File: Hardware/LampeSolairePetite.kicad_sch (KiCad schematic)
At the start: 30 parts, among them J1 CONN_ICSP, J2 Battery connector, J3 Connector_4p_r, P1 GREEN, P2 GREEN, P3 RED, P4 GREEN, U1 NCP114, U2 PIC16F1827

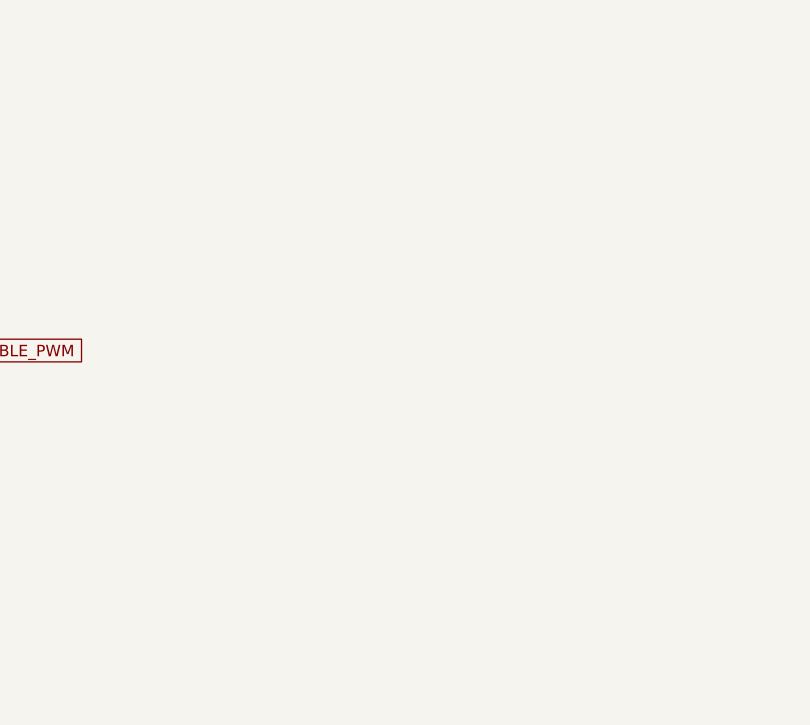
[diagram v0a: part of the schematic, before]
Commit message: Renamed files
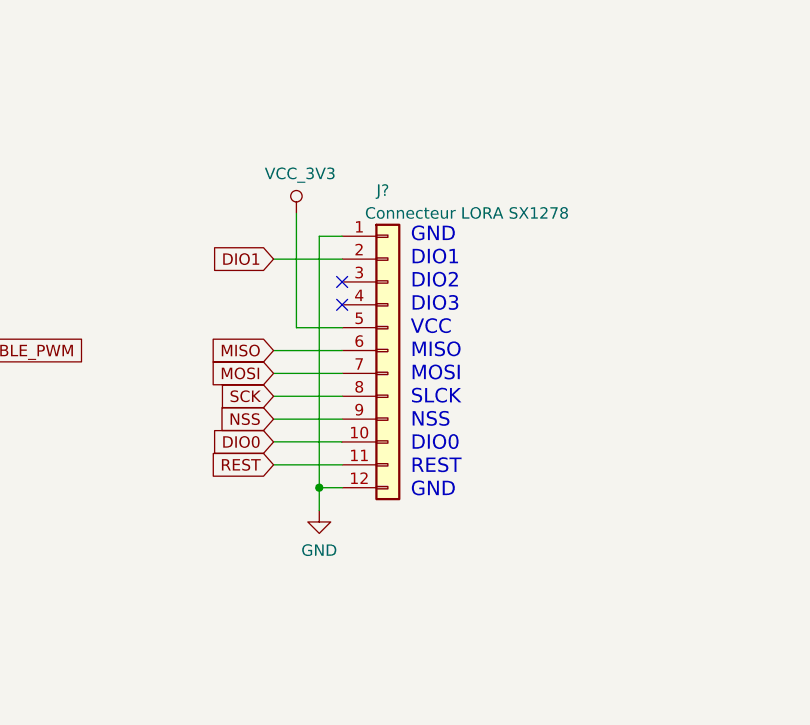
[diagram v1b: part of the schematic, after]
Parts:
- added J?: Connecteur LORA SX1278, Connector_PinHeader_1.27mm:PinHeader_1x12_P1.27mm_Vertical, symbol Connector_Generic:Conn_01x12
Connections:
- net DIO0: now also J?.10 (Pin_10)
- net DIO1: now also J?.2 (Pin_2)
- net GND: now also J?.1 (Pin_1), J?.12 (Pin_12)
- net MISO: now also J?.6 (Pin_6)
- net MOSI: now also J?.7 (Pin_7)
- net NSS: now also J?.9 (Pin_9)
- net REST: now also J?.11 (Pin_11)
- net SCK: now also J?.8 (Pin_8)
- net VCC_3V3: now also J?.5 (Pin_5)
- no-connect marks 2 -> 4
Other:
- note added: "GND DIO1 DIO2 DIO3 VCC MISO MOSI SLCK NSS DIO0 REST GND"

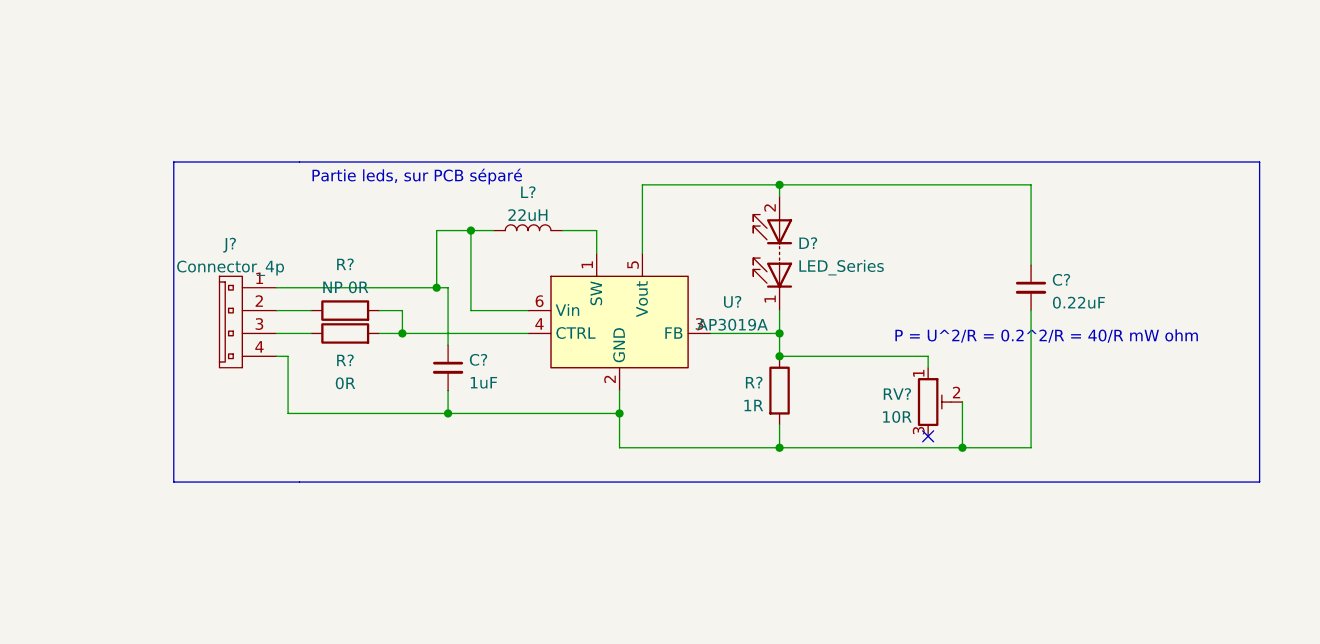
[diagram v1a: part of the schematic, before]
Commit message: created ledDriver schematic
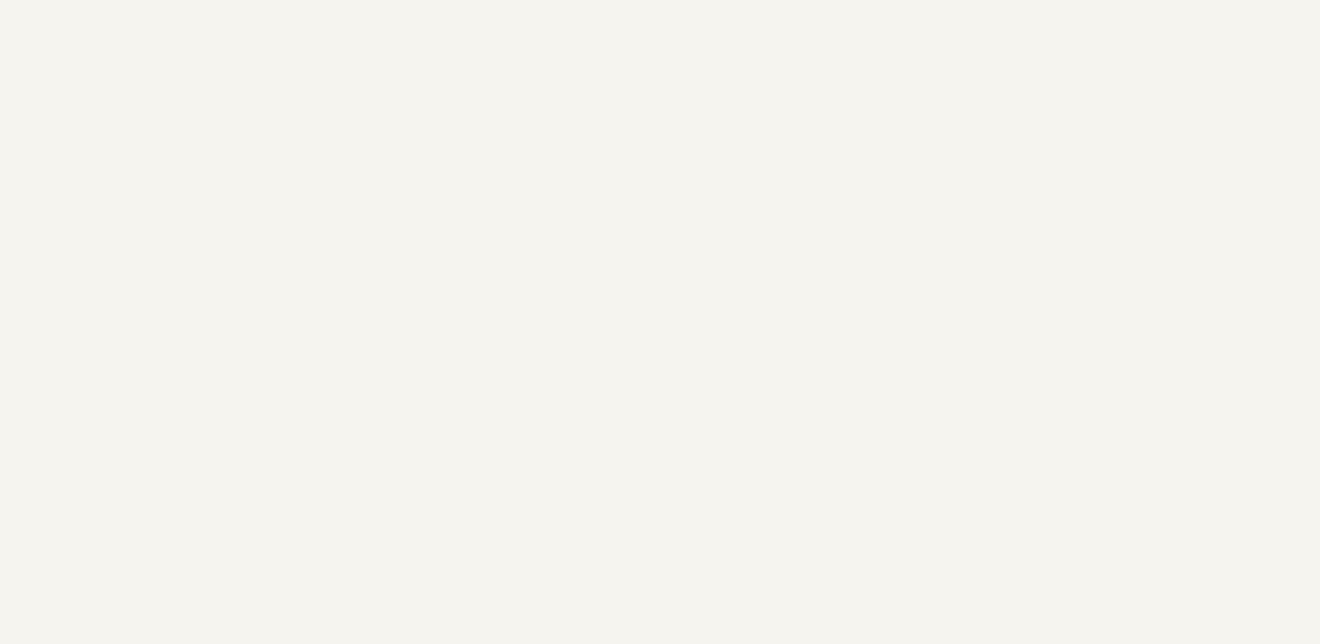
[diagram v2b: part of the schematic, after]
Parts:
- removed C?: 0.22uF, symbol Device:C_Small
- removed C?: 1uF, symbol Device:C_Small
- removed D?: LED_Series, symbol Device:LED_Series
- removed J?: Connector_4p, 0ESN_Lib:Connector_2p_m, symbol 0ESN_Lib:Connector_4p
- removed L?: 22uH, symbol Device:L
- removed R?: 0R, symbol Device:R
- removed R?: NP 0R, symbol Device:R
- removed R?: 1R, symbol Device:R
- removed RV?: 10R, symbol Device:R_Potentiometer_Trim
- removed U?: AP3019A, symbol 0ESN_Lib:AP3019A
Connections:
- no-connect marks 4 -> 3
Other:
- note removed: "P = U^2/R = 0.2^2/R = 40/R mW ohm"
- note removed: "Partie leds, sur PCB séparé"

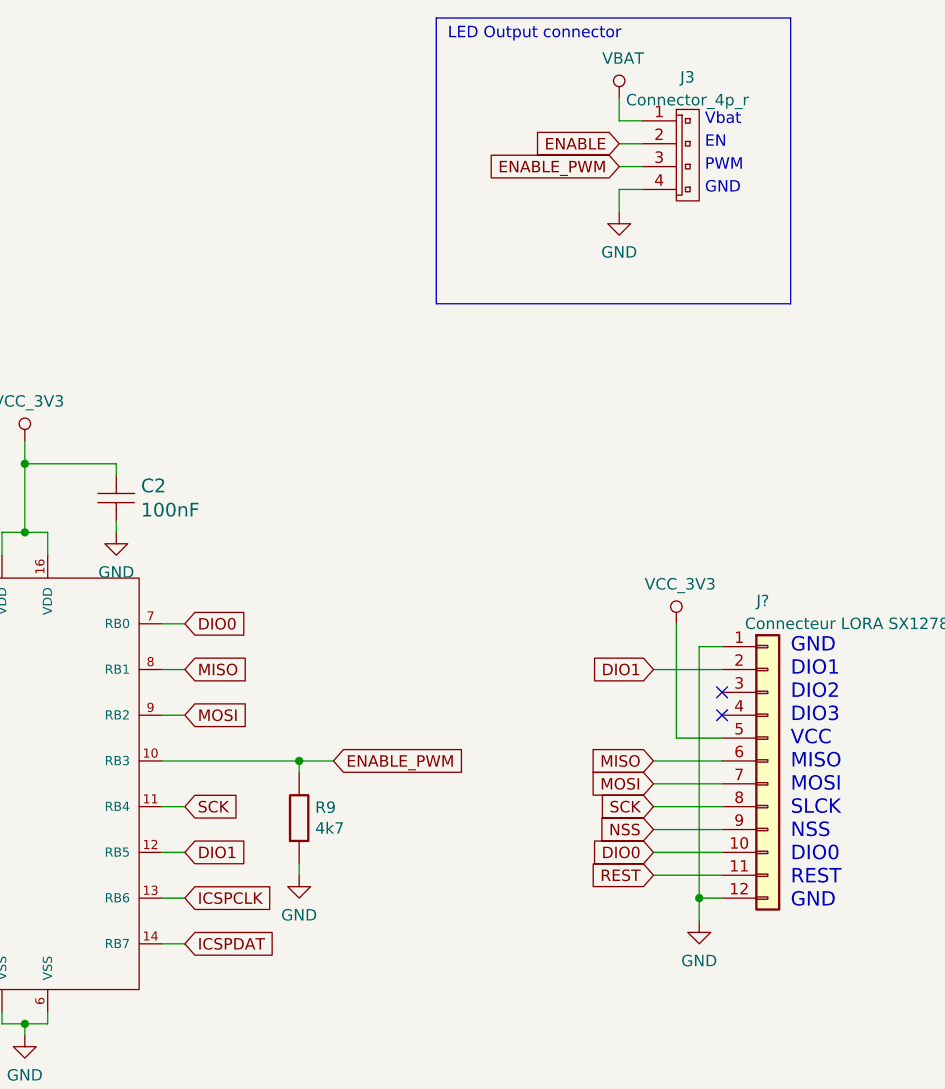
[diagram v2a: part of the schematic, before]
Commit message: PCB done for base card
Maybe add place for screws
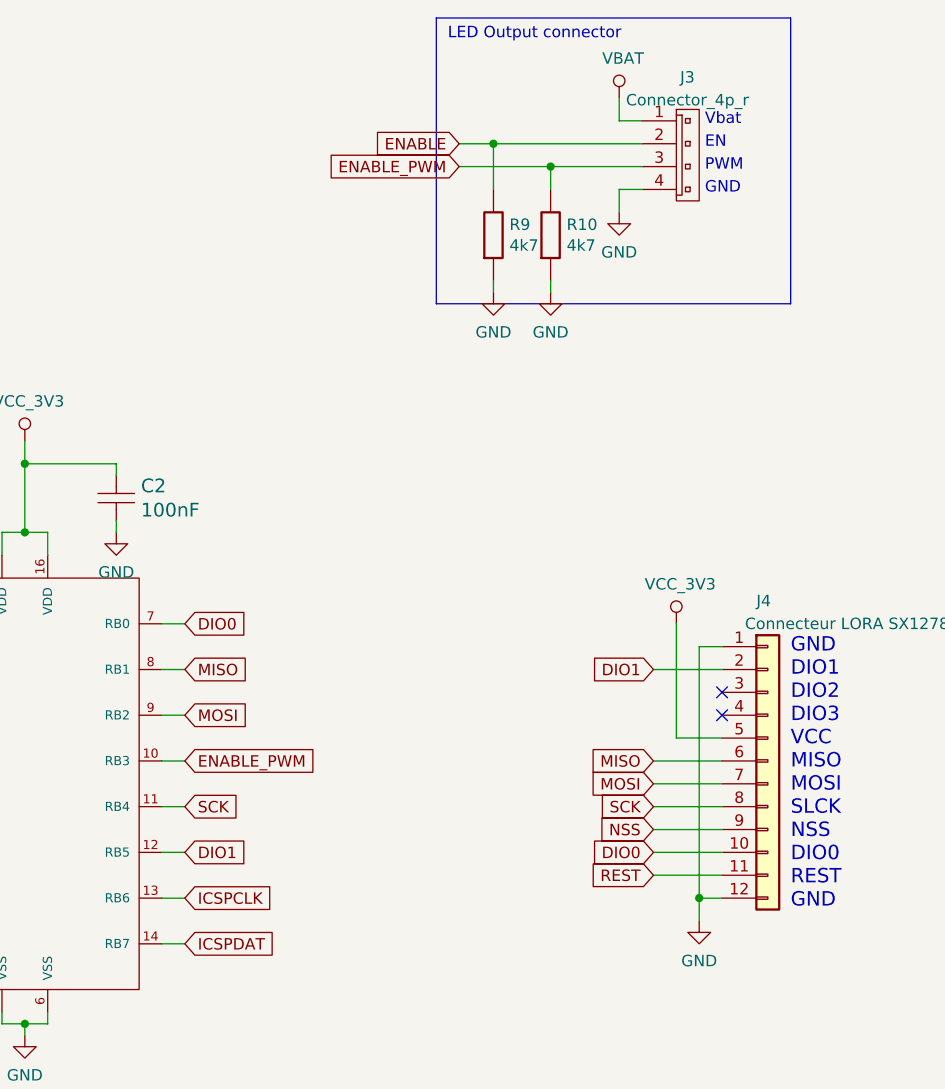
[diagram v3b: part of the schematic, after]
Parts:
- added R10: 4k7, Resistor_SMD:R_0805_2012Metric_Pad1.20x1.40mm_HandSolder, symbol LampeSolaire2-rescue:R-0EsseivaN_Lib
- C1, C2: footprint EsseivaN_Lib:C_0805_HandSoldering -> 0ESN_Lib:C_0805_2012Metric_Pad1.18x1.45mm_HandSolder
- J1: footprint EsseivaN_Lib:Pin_Header_Straight_1x05_Pitch2.54mm -> Connector_PinHeader_2.54mm:PinHeader_1x05_P2.54mm_Vertical
- J3: footprint 0ESN_Lib:Connector_2p_m -> 0ESN_Lib:Connector_4p_m
- P1, P2, P3, P4: footprint EsseivaN_Lib:D_0603_HandSoldering -> 0ESN_Lib:D_0603_1608Metric_Pad1.05x0.95mm_HandSolder
- R1, R2, R3, R4, R6, R7, R8, R9: footprint EsseivaN_Lib:R_0805_HandSoldering -> Resistor_SMD:R_0805_2012Metric_Pad1.20x1.40mm_HandSolder
- R5: footprint (none) -> Resistor_SMD:R_0805_2012Metric_Pad1.20x1.40mm_HandSolder
- U1: footprint (none) -> 0ESN_Lib:SOT-23-5_HandSoldering
- U2: footprint EsseivaN_Lib:SSOP-20_5.3x7.2mm_Pitch0.65mm -> Package_SO:SSOP-20_5.3x7.2mm_P0.65mm
- gave numbers to parts that had none: 1
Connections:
- net ENABLE: now also R9.1
- net ENABLE_PWM: now also R10.1; no longer R9.1
- net GND: now also R10.2

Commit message: edited libraries
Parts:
- C1, C2: symbol LampeSolaire2-rescue:CAPA-0EsseivaN_Lib -> 0ESN_Lib:C_Small
- J1: symbol LampeSolaire2-rescue:CONN_ICSP-0EsseivaN_Lib -> 0ESN_Lib:CONN_ICSP
- P1, P2, P3, P4: symbol LampeSolaire2-rescue:LED-0EsseivaN_Lib -> 0ESN_Lib:LED
- R1, R10, R2, R3, R4, R6, R7, R8, R9: symbol LampeSolaire2-rescue:R-0EsseivaN_Lib -> 0ESN_Lib:R
- R5: symbol Device:R -> 0ESN_Lib:R
- U2: symbol LampeSolaire2-rescue:PIC16F1827_20-0EsseivaN_Lib -> 0ESN_Lib:PIC16F1827_20
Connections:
- net VCC_3V3 renamed +3V3

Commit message: Finished lampe
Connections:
- net BATTERY_IND: now also P4.2 (K); no longer P4.1 (K)
- net GND: now also P1.2 (K); no longer P1.1 (K)
- net LED_GREEN: now also P2.2 (K); no longer P2.1 (K)
- net LED_RED: now also P3.2 (K); no longer P3.1 (K)
- net at R6.2: now also P4.1 (A); no longer P4.2 (A)
- net at R4.2: now also P3.1 (A); no longer P3.2 (A)
- net at R3.2: now also P2.1 (A); no longer P2.2 (A)
- net at R1.2: now also P1.1 (A); no longer P1.2 (A)
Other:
- moved on the sheet: P4
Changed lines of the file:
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@@
     (pin "6")
   )
-  (symbol (lib_id "0ESN_Lib:LED") (at 90.17 146.05 90) (unit 1)
-    (in_bom yes) (on_board yes) (fields_autoplaced)
-    (property "Reference" "P4" (id 0) (at 93.091 146.6613 90)
-      (effects (font (size 1.524 1.524)) (justify right))
-    )
-    (property "Value" "GREEN" (id 1) (at 93.091 149.6547 90)
-      (effects (font (size 1.524 1.524)) (justify right))
-    )
-    (property "Footprint" "0ESN_Lib:D_0603_1608Metric_Pad1.05x0.95mm_HandSolder" (id 2) (at 85.852 143.51 0)
-      (effects (font (size 1.27 1.27)) hide)
-    )
-    (property "Datasheet" "~" (id 3) (at 90.17 146.304 0)
+  (symbol (lib_name "LED_3") (lib_id "0ESN_Lib:LED") (at 90.17 146.05 270) (unit 1)
+    (in_bom yes) (on_board yes) (fields_autoplaced)
+    (property "Reference" "P4" (id 0) (at 92.202 146.6613 90)
+      (effects (font (size 1.524 1.524)) (justify left))
+    )
+    (property "Value" "GREEN" (id 1) (at 92.202 149.6547 90)
+      (effects (font (size 1.524 1.524)) (justify left))
+    )
+    (property "Footprint" "0ESN_Lib:D_0603_1608Metric_Pad1.05x0.95mm_HandSolder" (id 2) (at 94.488 148.59 0)
+      (effects (font (size 1.27 1.27)) hide)
+    )
+    (property "Datasheet" "~" (id 3) (at 90.17 146.05 0)
       (effects (font (size 1.27 1.27)) hide)
     )
@@
     (pin "2")
   )
-  (symbol (lib_id "0ESN_Lib:LED") (at 78.74 146.05 270) (mirror x) (unit 1)
+  (symbol (lib_id "0ESN_Lib:LED") (at 78.74 146.05 270) (unit 1)
     (in_bom yes) (on_board yes) (fields_autoplaced)
     (property "Reference" "P3" (id 0) (at 80.772 146.6613 90)
@@
       (effects (font (size 1.524 1.524)) (justify left))
     )
-    (property "Footprint" "0ESN_Lib:D_0603_1608Metric_Pad1.05x0.95mm_HandSolder" (id 2) (at 83.058 143.51 0)
-      (effects (font (size 1.27 1.27)) hide)
-    )
-    (property "Datasheet" "~" (id 3) (at 78.74 146.304 0)
-      (effects (font (size 1.27 1.27)) hide)
-    )
-    (pin "1")
-    (pin "2")
-  )
-  (symbol (lib_id "0ESN_Lib:LED") (at 64.77 146.05 270) (mirror x) (unit 1)
+    (property "Footprint" "0ESN_Lib:D_0603_1608Metric_Pad1.05x0.95mm_HandSolder" (id 2) (at 83.058 148.59 0)
+      (effects (font (size 1.27 1.27)) hide)
+    )
+    (property "Datasheet" "~" (id 3) (at 78.74 146.05 0)
+      (effects (font (size 1.27 1.27)) hide)
+    )
+    (pin "1")
+    (pin "2")
+  )
+  (symbol (lib_name "LED_2") (lib_id "0ESN_Lib:LED") (at 64.77 146.05 270) (unit 1)
     (in_bom yes) (on_board yes) (fields_autoplaced)
     (property "Reference" "P2" (id 0) (at 66.802 146.6613 90)
@@
       (effects (font (size 1.524 1.524)) (justify left))
     )
-    (property "Footprint" "0ESN_Lib:D_0603_1608Metric_Pad1.05x0.95mm_HandSolder" (id 2) (at 69.088 143.51 0)
-      (effects (font (size 1.27 1.27)) hide)
-    )
-    (property "Datasheet" "~" (id 3) (at 64.77 146.304 0)
+    (property "Footprint" "0ESN_Lib:D_0603_1608Metric_Pad1.05x0.95mm_HandSolder" (id 2) (at 69.088 148.59 0)
+      (effects (font (size 1.27 1.27)) hide)
+    )
+    (property "Datasheet" "~" (id 3) (at 64.77 146.05 0)
       (effects (font (size 1.27 1.27)) hide)
     )
@@
     (pin "2")
   )
-  (symbol (lib_id "0ESN_Lib:LED") (at 50.8 146.05 270) (mirror x) (unit 1)
+  (symbol (lib_name "LED_1") (lib_id "0ESN_Lib:LED") (at 50.8 146.05 270) (unit 1)
     (in_bom yes) (on_board yes) (fields_autoplaced)
     (property "Reference" "P1" (id 0) (at 52.832 146.6613 90)
@@
       (effects (font (size 1.524 1.524)) (justify left))
     )
-    (property "Footprint" "0ESN_Lib:D_0603_1608Metric_Pad1.05x0.95mm_HandSolder" (id 2) (at 55.118 143.51 0)
-      (effects (font (size 1.27 1.27)) hide)
-    )
-    (property "Datasheet" "~" (id 3) (at 50.8 146.304 0)
+    (property "Footprint" "0ESN_Lib:D_0603_1608Metric_Pad1.05x0.95mm_HandSolder" (id 2) (at 55.118 148.59 0)
+      (effects (font (size 1.27 1.27)) hide)
+    )
+    (property "Datasheet" "~" (id 3) (at 50.8 146.05 0)
       (effects (font (size 1.27 1.27)) hide)
     )
@@
   (symbol (lib_id "power:PWR_FLAG") (at 66.04 35.56 0) (unit 1)
     (in_bom yes) (on_board yes) (fields_autoplaced)
-    (property "Reference" "#FLG?" (id 0) (at 66.04 33.655 0)
+    (property "Reference" "#FLG0101" (id 0) (at 66.04 33.655 0)
       (effects (font (size 1.27 1.27)) hide)
     )
@@
   (symbol_instances
     (path "/415fb4d3-84d5-4bd3-9b82-c75cf816dd38"
-      (reference "#FLG?") (unit 1) (value "PWR_FLAG") (footprint "")
+      (reference "#FLG0101") (unit 1) (value "PWR_FLAG") (footprint "")
     )
     (path "/d23a0547-b184-4695-9ac0-fbf4224b0ab8"
